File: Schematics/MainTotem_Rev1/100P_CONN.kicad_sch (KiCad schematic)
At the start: 26 parts, among them J5 DF40C-100DS-0.4V_51_

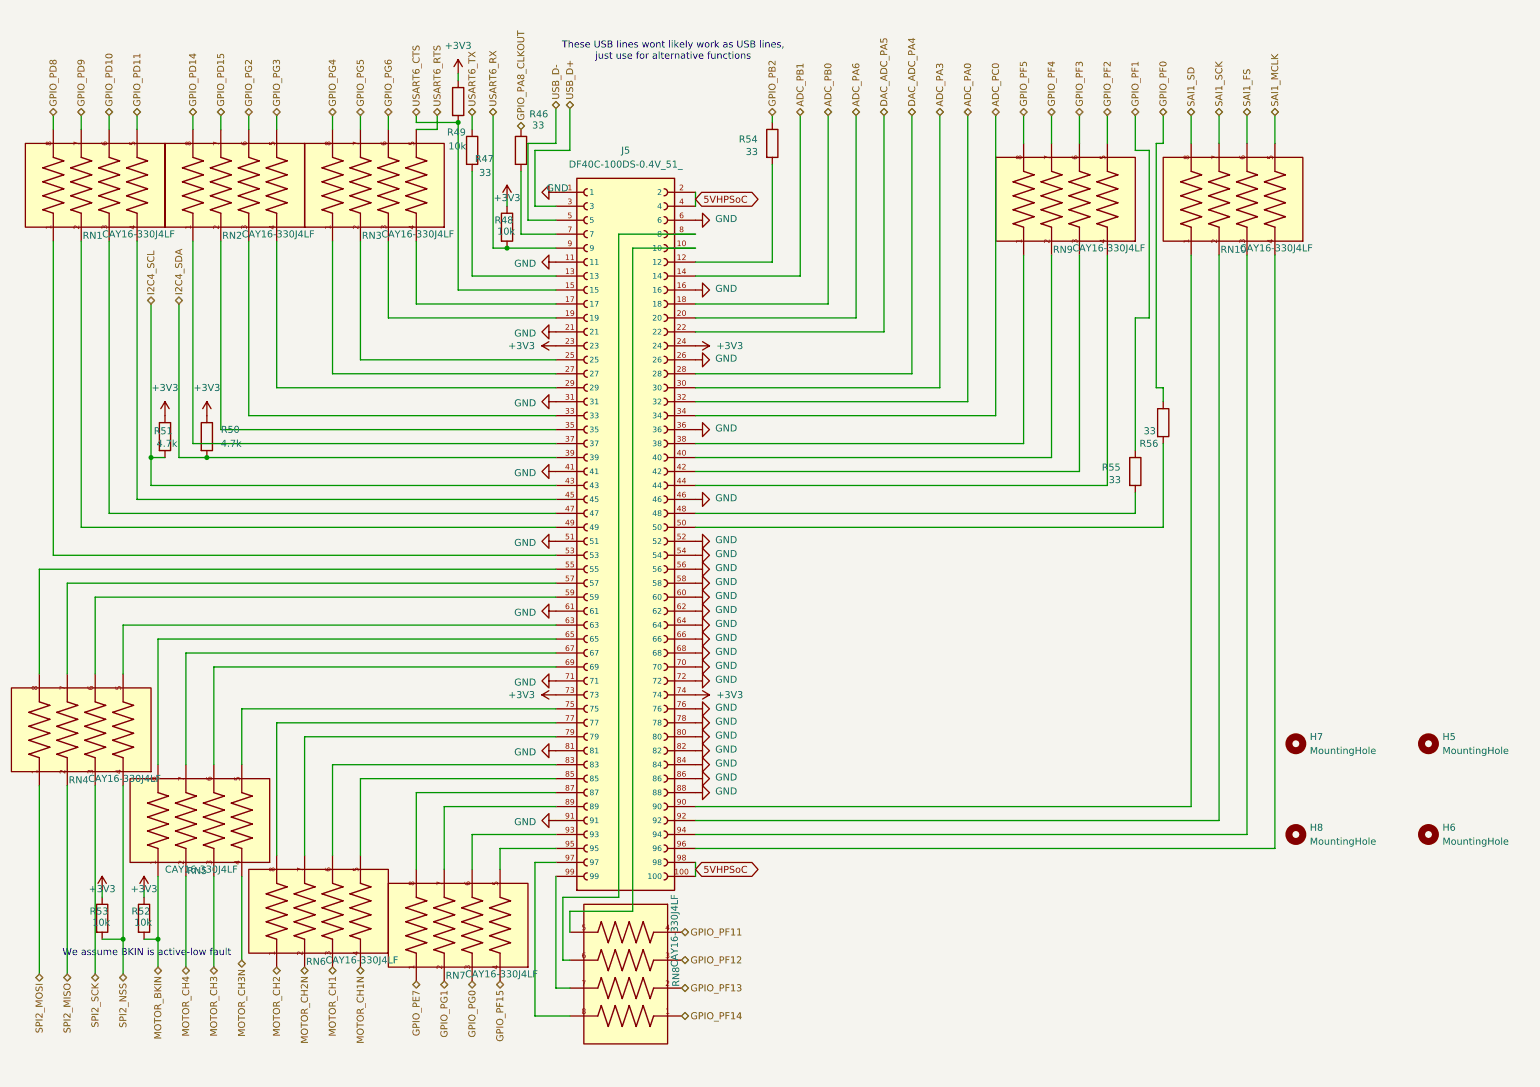
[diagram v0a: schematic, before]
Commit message: Layout Edits for Mezzanine Connector routing
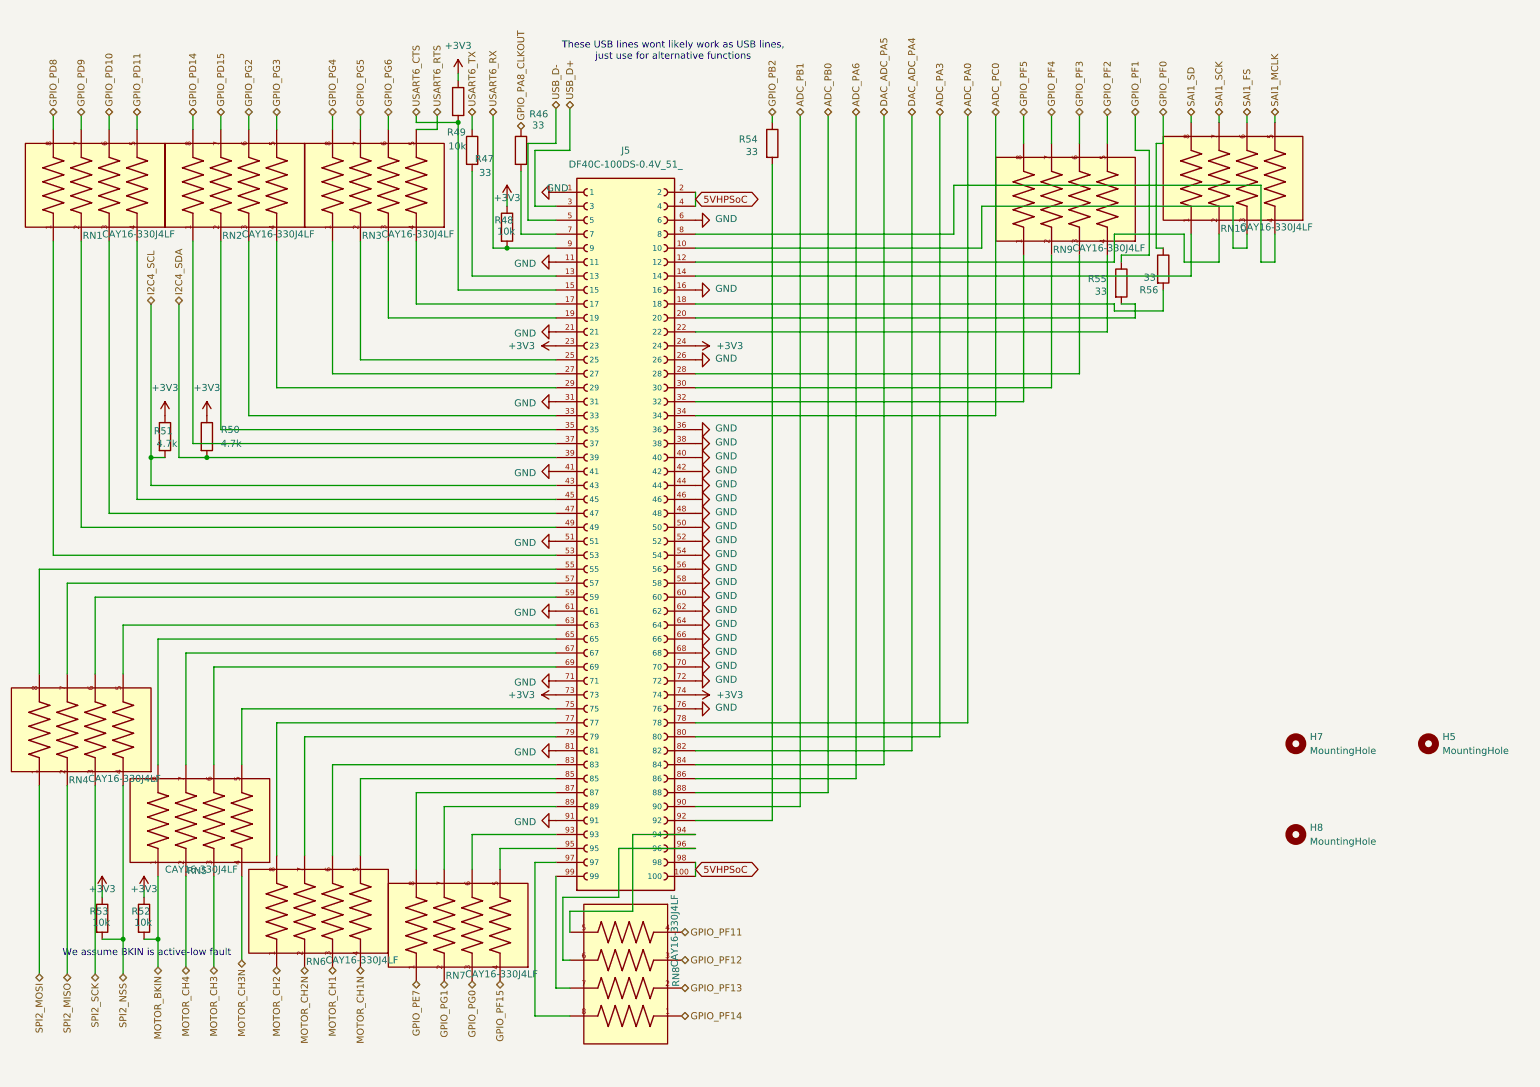
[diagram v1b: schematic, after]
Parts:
- removed H6: MountingHole, symbol Mechanical:MountingHole
- H5, H7, H8: footprint (none) -> MountingHole:MountingHole_3.2mm_M3_Pad_TopOnly
- J5: footprint DF40C-100DS-0.4V_51_:HIROSE_DF40C-100DS-0.4V_51_ -> 100pinMezzanineConnMale:HIROSE_DF40C-100DS-0.4V_51_
- R46, R47, R48, R49, R50, R51, R52, R53, R54, R55, R56: footprint (none) -> Resistor_SMD:R_0603_1608Metric_Pad0.98x0.95mm_HandSolder
- RN1, RN10, RN2, RN3, RN4, RN5, RN6, RN7, RN8, RN9: footprint CAY16-330J4LF:RESCAF80P320X160X60-8N -> 33ohmresistorarray:33ohmresarray
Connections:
- net ADC_PA0: now also J5.78; no longer J5.32
- net ADC_PA3: now also J5.80; no longer J5.30
- net ADC_PA6: now also J5.86; no longer J5.20
- net ADC_PB0: now also J5.88; no longer J5.18
- net ADC_PB1: now also J5.90; no longer J5.14
- net DAC_ADC_PA4: now also J5.82; no longer J5.28
- net DAC_ADC_PA5: now also J5.84; no longer J5.22
- net GND: now also J5.38, J5.40, J5.42, J5.44, J5.48, J5.50; no longer J5.78, J5.80, J5.82, J5.84, J5.86, J5.88
- net at J5.10: now also RN10.3; no longer RN8.5
- net at J5.12: now also RN10.2; no longer R54.2
- net at RN9.1: now also J5.32; no longer J5.38
- net at RN9.2: now also J5.30; no longer J5.40
- net at RN9.3: now also J5.28; no longer J5.42
- net at RN9.4: now also J5.22; no longer J5.44
- net at R55.2: now also J5.20; no longer J5.48
- net at R56.2: now also J5.18; no longer J5.50
- net at J5.8: now also RN10.4; no longer RN8.6
- net at RN10.1: now also J5.14; no longer J5.90
- net at J5.92: now also R54.2; no longer RN10.2
- net at J5.94: now also RN8.5; no longer RN10.3
- net at J5.96: now also RN8.6; no longer RN10.4
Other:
- moved on the sheet: R55, R56, RN10

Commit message: Rerouting layout to resolve collision issues
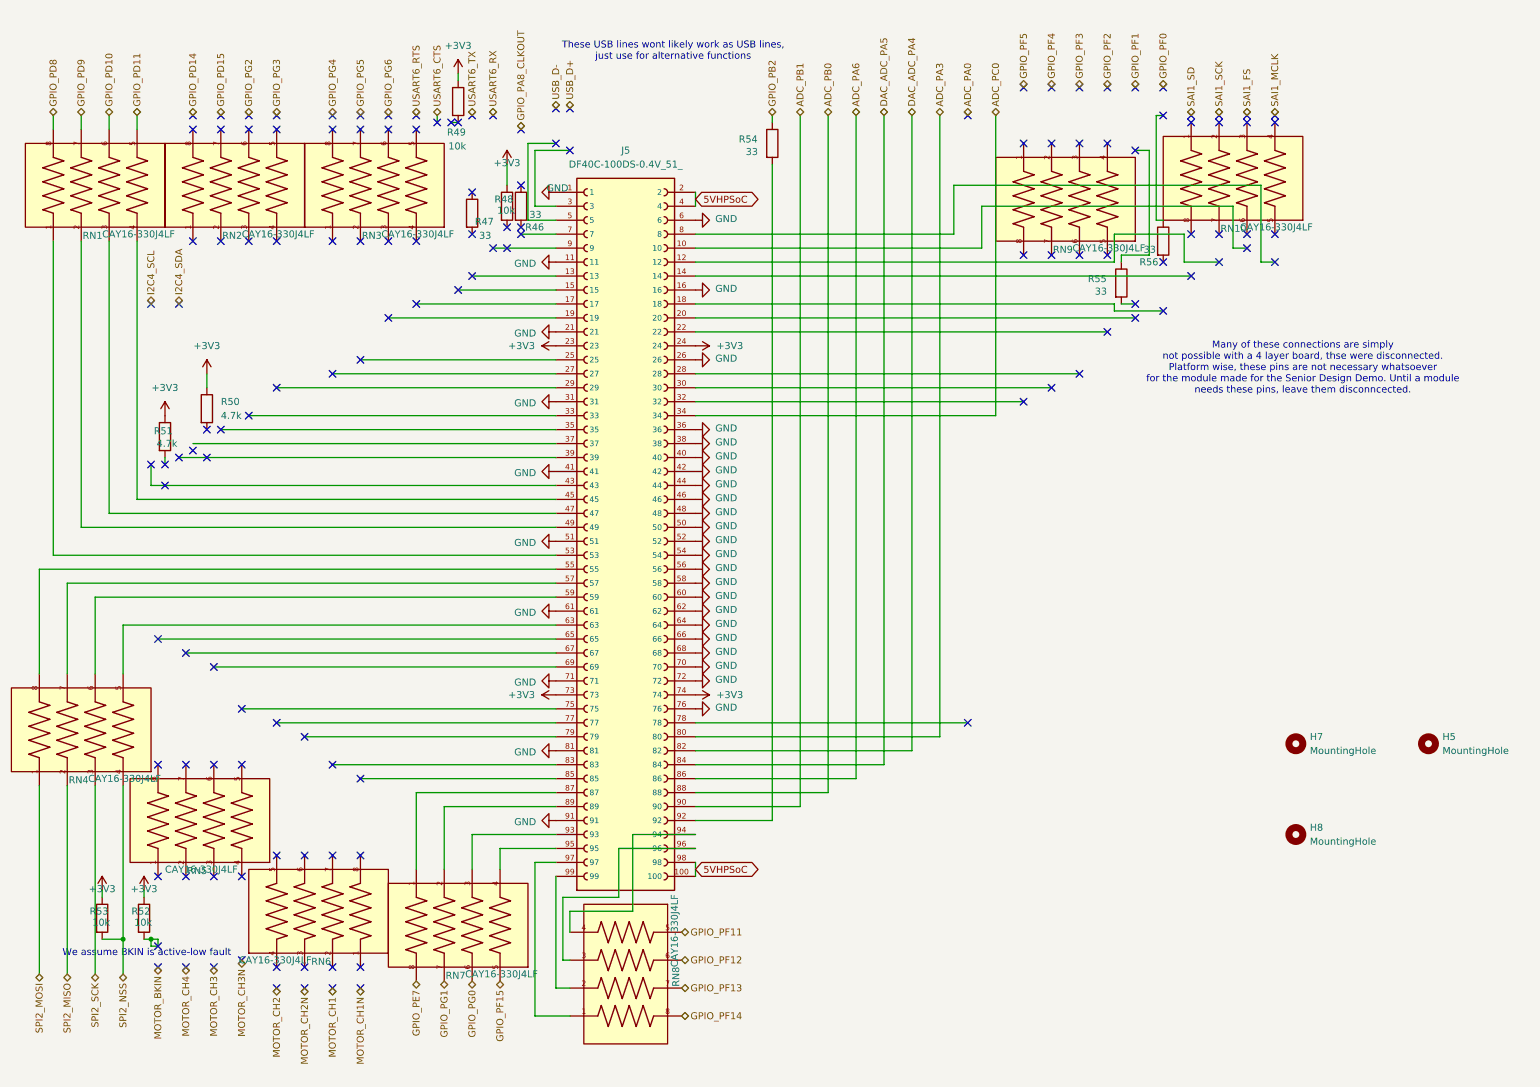
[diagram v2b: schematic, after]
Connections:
- net ADC_PA0: no longer J5.78
- net GPIO_PA8_CLKOUT: no longer R46.1
- net GPIO_PD14: no longer RN2.8
- net GPIO_PD15: no longer RN2.7
- net GPIO_PE7: now also RN7.8; no longer RN7.1
- net GPIO_PF0: no longer R56.1
- net GPIO_PF1: no longer R55.1
- net GPIO_PF11: now also RN8.5; no longer RN8.4
- net GPIO_PF12: now also RN8.6; no longer RN8.3
- net GPIO_PF13: now also RN8.7; no longer RN8.2
- net GPIO_PF14: now also RN8.8; no longer RN8.1
- net GPIO_PF15: now also RN7.5; no longer RN7.4
- net GPIO_PF2: no longer RN9.5
- net GPIO_PF3: no longer RN9.6
- net GPIO_PF4: no longer RN9.7
- net GPIO_PF5: no longer RN9.8
- net GPIO_PG0: now also RN7.6; no longer RN7.3
- net GPIO_PG1: now also RN7.7; no longer RN7.2
- net GPIO_PG2: no longer RN2.6
- net GPIO_PG3: no longer RN2.5
- net GPIO_PG4: no longer RN3.8
- net GPIO_PG5: no longer RN3.7
- net GPIO_PG6: no longer RN3.6
- net I2C4_SCL: no longer J5.43, R51.2
- net I2C4_SDA: no longer J5.39, R50.2
- net MOTOR_BKIN: no longer R52.2, RN5.1
- net MOTOR_CH1: no longer RN6.3
- net MOTOR_CH1N: no longer RN6.4
- net MOTOR_CH2: no longer RN6.1
- net MOTOR_CH2N: no longer RN6.2
- net MOTOR_CH3: no longer RN5.3
- net MOTOR_CH3N: no longer RN5.4
- net MOTOR_CH4: no longer RN5.2
- net SAI1_FS: no longer RN10.6
- net SAI1_MCLK: no longer RN10.5
- net SAI1_SCK: no longer RN10.7
- net SAI1_SD: no longer RN10.8
- net USART6_CTS: no longer J5.15, R49.2
- net USART6_RTS: no longer RN3.5
- net USART6_RX: no longer J5.9, R48.2
- net USART6_TX: no longer R47.1
- net USB_D+: no longer J5.3
- net USB_D-: no longer J5.5
- net at J5.95: now also RN7.4; no longer RN7.5
- net at J5.93: now also RN7.3; no longer RN7.6
- net at J5.89: now also RN7.2; no longer RN7.7
- net at J5.87: now also RN7.1; no longer RN7.8
- net at RN2.1: no longer J5.37
- net at RN2.2: no longer J5.35
- net at RN2.3: no longer J5.33
- net at RN2.4: no longer J5.29
- net at J5.10: no longer RN10.3
- net at J5.12: no longer RN10.2
- net at J5.13: no longer R47.2
- net at J5.14: no longer RN10.1
- net at J5.17: no longer RN3.4
- net at J5.18: no longer R56.2
- net at J5.19: no longer RN3.3
- net at J5.20: no longer R55.2
- net at J5.22: no longer RN9.4
- net at J5.25: no longer RN3.2
- net at J5.27: no longer RN3.1
- net at J5.28: no longer RN9.3
- net at J5.30: no longer RN9.2
- net at J5.32: no longer RN9.1
- net at J5.65: no longer RN5.8
- net at J5.67: no longer RN5.7
- net at J5.69: no longer RN5.6
- net at J5.7: no longer R46.2
- net at J5.75: no longer RN5.5
- net at J5.77: no longer RN6.8
- net at J5.79: no longer RN6.7
- net at J5.8: no longer RN10.4
- net at J5.83: no longer RN6.6
- net at J5.85: no longer RN6.5
- net at J5.94: now also RN8.4; no longer RN8.5
- net at J5.96: now also RN8.3; no longer RN8.6
- net at J5.97: now also RN8.1; no longer RN8.8
- net at J5.99: now also RN8.2; no longer RN8.7
- no-connect marks 0 -> 135
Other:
- note added: "Many of these connections are simply not possible with a 4 layer board, thse were disconnected. Platform wise, these pins are not necessary whatsoever for the module made for the Senior Design Demo. Until a module needs these pins, leave them disconncected."
- moved on the sheet: R46, R47, R48, R50, R56, RN6
